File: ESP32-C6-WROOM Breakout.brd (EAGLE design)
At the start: 96.8 x 49.5 mm, 65 parts, among them J10 HP I2C, J11 LP I2C, J2 LP I2C, P1 GPIO-A2, P10 LP_I2C, P11 LiPo In, P2 GPIO-A1, P3 ADC, P4 O/P DRV, P5 CTRL, P6 HP_UART, P7 HP_I2C, P8 B2B-PH-K, P9 B2B-PH-K, U1 AP2112K-3.3TRG1, U2 ESP32-C6-WROOM-1-N4, U3 AP2112K-3.3TRG1LONG_PADS

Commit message: gitignore + WIP (close to candidate v1)
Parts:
- removed Q1, Q2, Q3, Q4: (no value), Master 2016:SOT23
- removed U1: AP2112K-3.3TRG1, AP2112K-3.3TRG1:SOT95P285X140-5N
- added J3: HP_UART, Connector:5P-2.54
- added Q6, Q7, Q8: (no value), Master 2016:SOT23_LONG
- U3: value AP2112K-3.3TRG1LONG_PADS -> AP2112
- moved P1 27.9 mm to (90.2, 3.81)
- moved JP7 10.2 mm to (64.8, 11.4)
- moved P2 10.2 mm to (64.8, 3.81)
- moved P6 10.2 mm to (78.7, 3.81)
- moved JP1 10.2 mm to (62.2, 11.4)
- moved JP8 10.2 mm to (67.3, 11.4)
- moved J10 7.75 mm to (28.6, 20.3)
- moved C7 6.75 mm to (32.4, 29.2), turned to 90 degrees
- moved U3 6.35 mm to (22.9, 29.2), turned to 270 degrees
- moved JP6 4.26 mm to (54.6, 23.5)
- moved C3 2.84 mm to (14.0, 29.2), flipped to the top
- moved C6 1.42 mm to (27.3, 29.2), turned to 90 degrees
- moved C8 1.27 mm to (19.1, 29.2), turned to 270 degrees
- moved D1 0.90 mm to (15.2, 37.5)
- moved P11 0.64 mm to (3.17, 44.5)
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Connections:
- net GND: now also J3.1; no longer U1.2
- net GPIO22: now also Q8.1; no longer Q2.1
- net GPIO23: now also Q6.1; no longer Q4.1
- net LP_GPIO4: now also Q7.1; no longer Q3.1
- net LP_GPIO5: no longer Q1.1
- net N$12: now also Q7.3; no longer Q3.3
- net N$13: no longer U1.5
- net N$15: now also Q6.3; no longer Q4.3
- net N$7: no longer Q1.3
- net RX: now also J3.4
- net TX: now also J3.5
- net UART_VCC: now also J3.3, Q8.3; no longer Q2.3
- net VCC: now also Q6.2, Q7.2, Q8.2; no longer Q1.2, Q2.2, Q3.2, Q4.2
- net VIN: no longer U1.1, U1.3
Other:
- board text added: "3V3"
- board text added: "ADC / #2"
- board text added: "GND"
- board text added: "SCL"
- board text added: "SDA"

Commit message: WIP getting there
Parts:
- added P12: Pwr Out, con-jst-ph:B3B-PH-K
- added P13: (no value), Master 2016:1X02
- added Q1: FDN338P, Master 2016:SOT23_LONG
- added R12, R13, R14, R15, R21: (no value), Master 2016:1206
- added R16, R17, R18, R19: 4k7, Master 2016:1206
- added R20: 10k, Master 2016:1206
- BAT1: value (none) -> 2-1775485-1
- C1, C2: value (none) -> 18p
- C3: value (none) -> 10u
- JP10: value BOOT -> (none)
- JP12: value (none) -> UART Vcc; device Master 2016:1X02 -> Connector:3P-2.54
- JP8: value (none) -> BOOT
- JP9: value (none) -> I_measure
- P1: value GPIO-A2 -> LP_I2C; device con-jst-eh:B3B-EH-A -> con-jst-eh:B4B-EH-A
- P10: value LP_I2C -> Pwr Sw 23; device con-jst-eh:B4B-EH-A -> con-jst-ph:B2B-PH-K
- P2: value GPIO-A1 -> HP_I2C; device con-jst-eh:B5B-EH-A -> con-jst-eh:B4B-EH-A
- P3: value ADC -> CTRL
- P5: value CTRL -> ADC; device con-jst-eh:B3B-EH-A -> con-jst-eh:B4B-EH-A
- P6: value HP_UART -> GPIO-A1; device con-jst-eh:B4B-EH-A -> con-jst-eh:B5B-EH-A
- P7: value HP_I2C -> HP_UART
- P8: value B2B-PH-K -> GPIO-A2; device con-jst-ph:B2B-PH-K -> con-jst-eh:B3B-EH-A
- P9: value B2B-PH-K -> Pwr Sw 22
- Q5, Q6, Q7, Q8: value (none) -> FDN338P
- R3, R5, R6, R8: value (none) -> 10k
- X1: value (none) -> CFS-20632768EZFB
- moved P10 90.4 mm to (92.7, 34.3), turned to 90 degrees
- moved P1 82.5 mm to (7.62, 3.81)
- moved P7 61.0 mm to (81.3, 3.81)
- moved JP10 48.6 mm to (88.9, 47.0)
- moved P2 44.4 mm to (20.3, 3.81)
- moved JP5 42.3 mm to (46.4, 12.1), turned to 90 degrees
- moved JP6 32.4 mm to (84.5, 10.8)
- moved JP8 30.0 mm to (43.2, 29.2), turned to 180 degrees
- moved JP7 27.8 mm to (84.5, 31.1), turned to 0 degrees
- moved P5 21.6 mm to (53.3, 3.81)
- moved P3 20.3 mm to (31.8, 3.81)
- moved P9 19.7 mm to (92.7, 13.3)
- moved JP12 18.5 mm to (95.9, 23.5)
- moved JP2 17.8 mm to (66.0, 11.4)
- moved JP3 15.9 mm to (68.6, 11.4), turned to 90 degrees
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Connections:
- new net LP_GPIO6: U2.6
- new net LP_GPIO7: U2.7
- new net N$9: P5.4, Q1.3
- new net PWR_SW_22: JP12.1, JP6.2, P9.2, Q8.3
- net ADC: now also P5.2; no longer P3.2
- net GND: now also JP2.2, JP3.2, P1.2, P10.1, P12.1, P2.2, P7.1; no longer JP10.2, JP7.2, P1.1, P10.2, P2.1, P7.2
- net GPIO10: now also P2.3, R18.1; no longer P7.3
- net GPIO11: now also P2.4, R19.1; no longer P7.4
- net GPIO15_R: now also JP10.2, P3.2; no longer JP11.2, P5.2
- net GPIO18: now also P6.2; no longer P2.2
- net GPIO19: now also JP2.1, P6.3; no longer JP7.1, P2.3
- net GPIO20: now also JP3.1, P6.4; no longer JP8.1, P2.4
- net GPIO21: now also P6.5, R2.1; no longer P2.5
- net GPIO22: now also P8.3, R15.1, R15.2; no longer P1.3, R2.1
- net GPIO23: now also P8.2, R14.1, R14.2; no longer P1.2
- net GPIO6: now also P1.4, Q1.1, R16.2, R20.1, R21.1, R21.2; no longer P10.4, U2.6
- net GPIO7: now also P1.3, R17.2; no longer P10.3, U2.7
- net GPIO8: now also P13.1; no longer JP6.1
- net GPIO9: now also P13.2; no longer JP6.2
- net LP_GPIO3: now also P3.3; no longer P5.3
- net LP_GPIO4: now also R13.1, R13.2
- net LP_GPIO5: now also JP5.2, R12.1, R12.2; no longer JP2.2
- net LP_GPIO5_P: now also JP5.1; no longer JP2.1
- net N$1: now also JP8.1; no longer JP10.1
- net N$10: now also JP11.2; no longer JP12.2
- net N$11: now also JP11.1; no longer JP12.1
- net N$15: now also JP7.2, P10.2; no longer JP5.2, P9.2
- net N$8: now also JP10.1; no longer JP11.1
- net RX: now also P7.3; no longer P6.3
- net TX: now also P7.2; no longer P6.2
- net UART_VCC: now also JP12.2, P7.4; no longer JP3.2, P6.4, P8.2, Q8.3
- net VCC: now also JP12.3, JP6.1, JP7.1, P1.1, P12.2, P2.1, P5.3, Q1.2, R16.1, R17.1, R18.2, R19.2, R20.2; no longer JP3.1, JP5.1, P10.1, P3.3, P7.1
- net VIN: now also P12.3
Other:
- board size 96.8 x 49.5 mm -> 99 x 49.5 mm
- board text added: "ADC"
- board text removed: "ADC / #2"

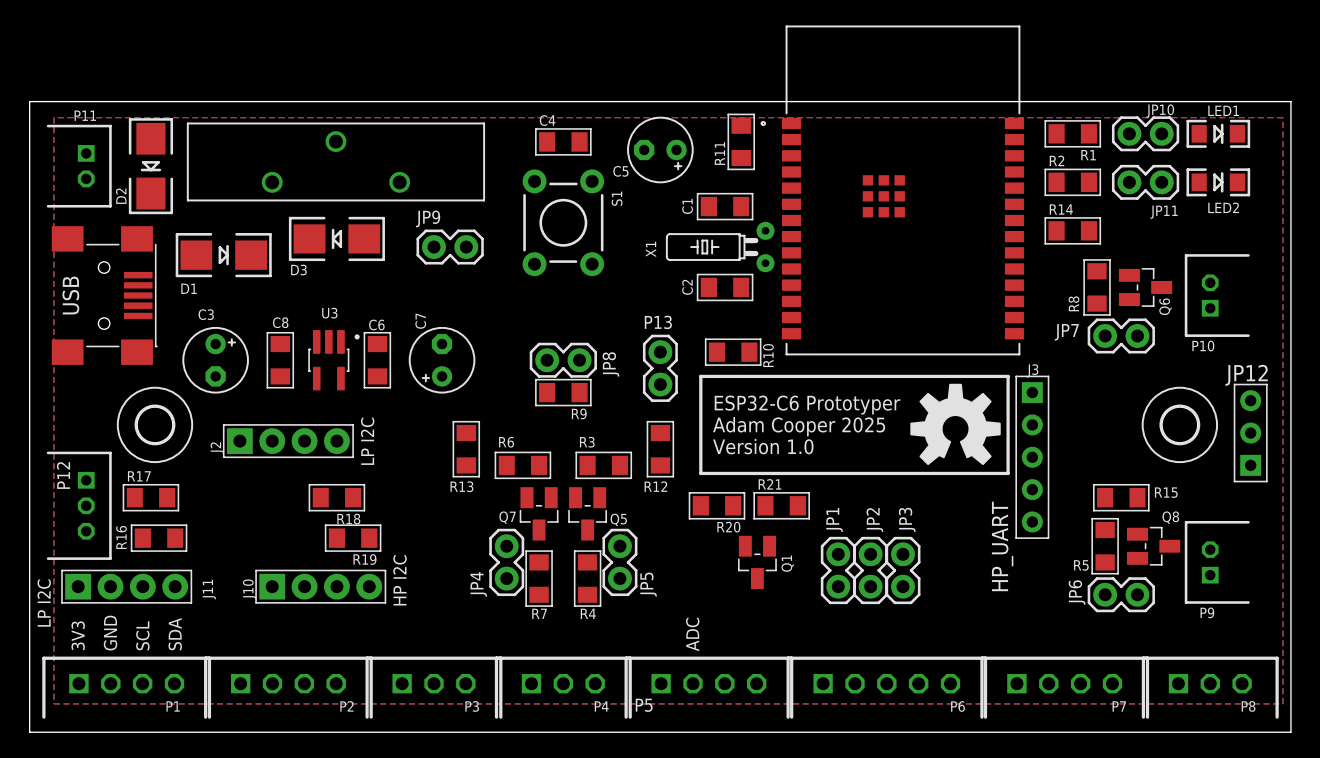
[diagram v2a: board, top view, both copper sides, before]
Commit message: move ADC and add o/p drive caps
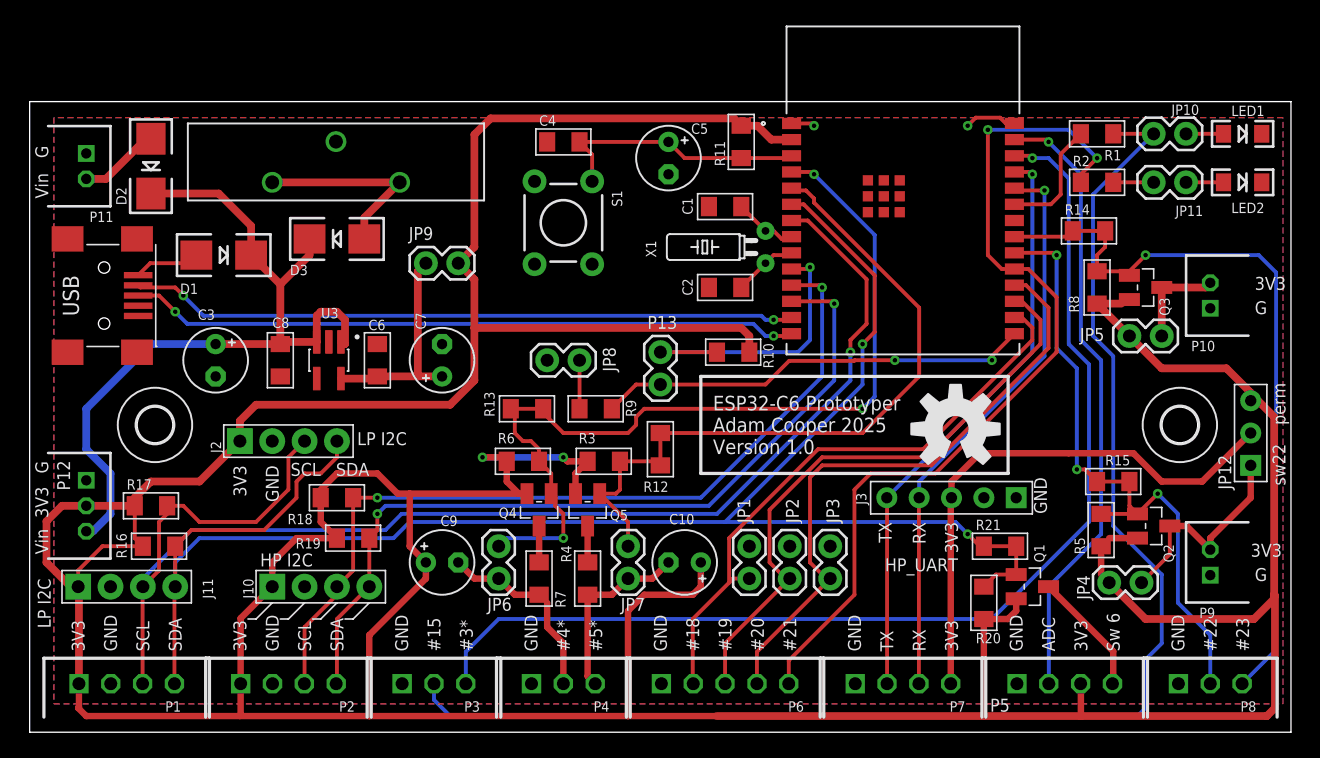
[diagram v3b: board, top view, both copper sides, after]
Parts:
- removed Q7, Q8: FDN338P, Master 2016:SOT23_LONG
- added C10, C9: 10u, Master 2016:E2,5-5
- added LOGO2: OSHW-LOGOL, Master 2016:OSHW-LOGO-L
- added Q2, Q4: FDN338P, Master 2016:SOT23_LONG
- P4: value O/P DRV -> HI DRV/CNT
- moved JP6 47.6 mm to (36.8, 12.1), turned to 90 degrees
- moved JP4 47.3 mm to (84.8, 11.7), turned to 0 degrees
- moved JP5 44.3 mm to (86.4, 31.1), turned to 0 degrees
- moved JP7 42.0 mm to (47.0, 12.1), turned to 90 degrees
- moved P5 27.9 mm to (81.3, 3.81)
- moved R20 22.3 mm to (74.9, 10.2), turned to 270 degrees
- moved Q1 21.7 mm to (78.7, 11.4), turned to 270 degrees
- moved R21 17.4 mm to (76.2, 14.6)
- moved P6 12.7 mm to (54.6, 3.81)
- moved P7 12.7 mm to (68.6, 3.81)
- moved J3 7.10 mm to (72.4, 18.4), turned to 270 degrees
- moved JP1 7.01 mm to (56.5, 12.1)
- moved JP2 6.38 mm to (59.7, 12.1)
- moved JP3 5.75 mm to (62.9, 12.1)
- moved R13 5.72 mm to (39.1, 25.4), turned to 0 degrees
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- renumbered Q6 to Q3
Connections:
- net N$16 renamed GPIO15
- removed net GPIO6: J11.4, J2.4, P1.4, Q1.1, R16.2, R20.1, R21.1, R21.2
- removed net GPIO7: J11.3, J2.3, P1.3, R17.2
- net GPIO22: now also P8.2, Q2.1; no longer P8.3, Q8.1
- net GPIO23: now also P8.3; no longer P8.2
- net LP_GPIO4: now also JP6.2, Q4.1; no longer JP4.2, Q7.1
- net LP_GPIO4_P: now also C9.-, JP6.1; no longer JP4.1
- net LP_GPIO5: now also JP7.2; no longer JP5.2
- net LP_GPIO5_P: now also C10.-, JP7.1; no longer JP5.1
- net LP_GPIO6: now also J11.4, J2.4, P1.4, Q1.1, R16.2, R20.1, R21.1, R21.2
- net LP_GPIO7: now also J11.3, J2.3, P1.3, R17.2
- net N$12: now also Q4.3; no longer Q7.3
- net N$15: now also JP5.2; no longer JP7.2
- net PWR_SW_22: now also JP4.2, Q2.3; no longer JP6.2, Q8.3
- net VCC: now also C10.+, C9.+, JP4.1, JP5.1, Q2.2, Q4.2; no longer JP6.1, JP7.1, Q7.2, Q8.2
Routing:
- net VCC: track 0.00 -> 403.2 mm, vias 0 -> 2
- net LP_GPIO6: track 0.00 -> 136.7 mm, vias 0 -> 2
- net GPIO15_R: track 0.00 -> 110.9 mm
- net LP_GPIO7: track 0.00 -> 109.1 mm, vias 0 -> 1
- net LP_GPIO3: track 0.00 -> 88.3 mm, vias 0 -> 1
- net GPIO21: track 0.00 -> 70.9 mm, vias 0 -> 2
- net LP_GPIO4: track 0.00 -> 70.0 mm, vias 0 -> 3
- net GPIO10: track 0.00 -> 66.4 mm, vias 0 -> 2
- net GPIO11: track 0.00 -> 64.4 mm, vias 0 -> 2
- net VIN: track 0.00 -> 62.4 mm
- net GPIO23: track 0.00 -> 60.3 mm, vias 0 -> 1
- net LP_GPIO5: track 0.00 -> 56.5 mm
- net GPIO13: track 0.00 -> 52.7 mm, vias 0 -> 2
- net GPIO12: track 0.00 -> 52.5 mm, vias 0 -> 2
- net GPIO22: track 0.00 -> 49.9 mm, vias 0 -> 3
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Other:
- board text added: "#10"
- board text added: "#11"
- board text added: "#15"
- board text added: "#18"
- board text added: "#19"
- board text added: "#2*"
- board text added: "#20"
- board text added: "#21"
- board text added: "#22"
- board text added: "#23"
- board text added: "#3*"
- board text added: "#4*"
- board text added: "#5*"
- board text added: "#6*"
- board text added: "#7*"
- board text added: "G"
- board text added: "RX"
- board text added: "Sw 6"
- board text added: "TX"
- board text added: "Vin"
- board text added: "perm"
- board text added: "sw22"

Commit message: 32kHz crystal ground plane separation
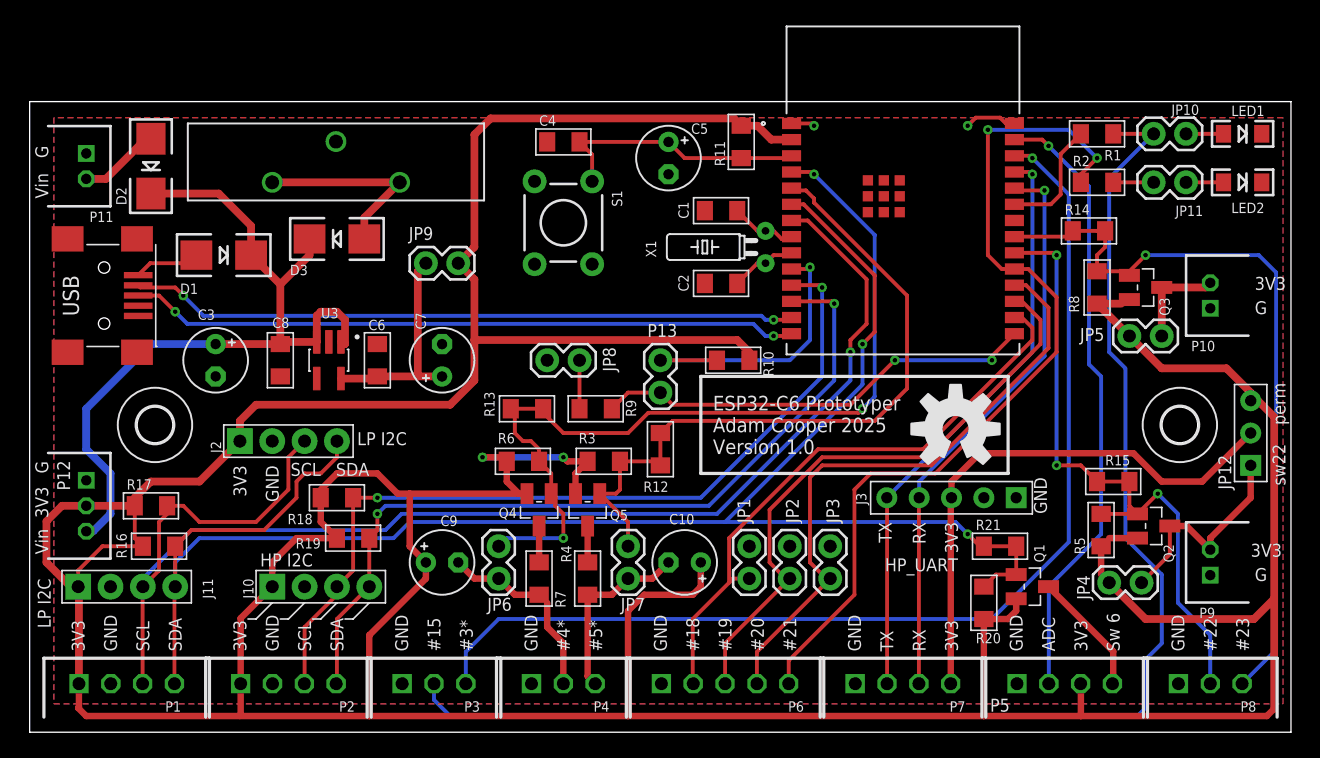
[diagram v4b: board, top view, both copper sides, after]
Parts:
- moved P13 0.63 mm to (49.5, 29.2)
- moved R10 0.63 mm to (55.2, 29.2)
- moved C2 0.45 mm to (54.3, 35.2)
- moved C1 0.45 mm to (54.3, 41.0)
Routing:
- net LP_GPIO3: track 88.3 -> 86.2 mm
- net GPIO15_R: track 110.9 -> 109.9 mm
- net VCC: track 403.2 -> 402.3 mm
- net LP_GPIO5: track 56.5 -> 55.7 mm
- net GPIO9: track 34.2 -> 35.0 mm
- net GPIO22: track 49.9 -> 50.7 mm

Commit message: close to v1 rev
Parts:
- removed Q5: FDN338P, Master 2016:SOT23_LONG
- added D4: SL115B, Master 2016:DO-214AA
- added J4, J5: (no value), Connector:1P-65/35MIL
- added JP13: PS Src, Connector:3P-2.54
- added JP14: I_measure, Master 2016:1X02
- added P14: Backup, con-jst-ph:B2B-PH-K
- C10: device Master 2016:E2,5-5 -> Master 2016:1206
- C3, C9: value 10u -> 100n; device Master 2016:E2,5-5 -> Master 2016:1206
- C6: value 100n -> 1u
- C7: value 10u -> 1u; device Master 2016:E2,5-5 -> Master 2016:1206
- C8: value 100n -> 10u
- J2: value LP I2C -> HP I2C
- JP3: value (none) -> BOOT
- JP8: value BOOT -> (none)
- JP9: value I_measure -> (none)
- P10: device con-jst-ph:B2B-PH-K -> con-jst-ph:B3B-PH-K
- P5: device con-jst-eh:B4B-EH-A -> con-jst-eh:B3B-EH-A
- P6: device con-jst-eh:B5B-EH-A -> con-jst-eh:B6B-EH-A
- R20: value 10k -> 2k2
- R21: value (none) -> 1k
- moved R21 63.3 mm to (15.2, 31.8)
- moved R20 62.5 mm to (15.2, 28.6), turned to 0 degrees
- moved C9 60.9 mm to (83.2, 47.0)
- moved Q3 50.7 mm to (40.0, 17.5), turned to 180 degrees
- moved C3 45.2 mm to (56.8, 45.4)
- moved C10 28.0 mm to (79.4, 14.6), turned to 0 degrees
- moved JP9 27.6 mm to (47.0, 14.3), turned to 270 degrees
- moved JP3 26.1 mm to (43.2, 29.2), turned to 180 degrees
- moved Q1 24.8 mm to (86.7, 34.9)
- moved R11 20.7 mm to (36.2, 40.0), turned to 180 degrees
- moved C8 18.2 mm to (34.3, 18.4), turned to 180 degrees
- moved JP8 16.2 mm to (36.8, 14.3), turned to 270 degrees
- moved C6 6.35 mm to (21.0, 29.2), turned to 270 degrees
- moved R2 4.72 mm to (87.3, 40.0)
- moved R1 3.93 mm to (82.9, 43.2)
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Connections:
- new net N$14: JP13.3, P10.3
- new net N$16: J4.P$1, JP1.1
- new net N$2: D2.A, P11.1
- new net N$5: JP13.2, JP5.1, Q1.2, R8.2
- net ADC: now also C9.1, R20.1, R21.1
- net GND: now also C10.1, C3.2, C7.2, C9.2, P10.2, P11.2, P12.2, P14.2, P9.2, R20.2; no longer C3.-, C7.-, JP8.2, P10.1, P11.1, P12.1, P9.1
- net GPIO10: now also J2.3
- net GPIO11: now also J2.4
- net GPIO18: no longer JP1.1
- net GPIO19: no longer JP2.1
- net GPIO20: no longer JP3.1
- net GPIO23: now also Q1.1; no longer Q3.1
- net LP_GPIO4: now also Q3.1; no longer Q4.1
- net LP_GPIO4_P: now also JP8.2; no longer C9.-
- net LP_GPIO5: now also Q4.1; no longer Q5.1
- net LP_GPIO5_P: now also JP9.2; no longer C10.-
- net LP_GPIO6: no longer J2.4, Q1.1, R20.1, R21.1, R21.2
- net LP_GPIO7: no longer J2.3
- net N$1: now also JP3.1; no longer JP8.1
- net N$12: now also JP8.1, Q3.3; no longer Q4.3
- net N$13: now also C7.1, D3.C, JP14.1; no longer C6.1, C7.+, JP9.1
- net N$15: now also P10.1, Q1.3; no longer P10.2, Q3.3
- net N$4: now also D4.A, P14.1; no longer D2.A, P11.2
- net N$7: now also JP9.1, Q4.3; no longer Q5.3
- net N$9: now also J5.P$1, JP2.1; no longer P5.4, Q1.3
- net PWR_SW_22: now also P9.1; no longer P9.2
- net VCC: now also C10.2, C3.1, C8.1, JP13.1, JP14.2, P12.1, P6.6; no longer C10.+, C9.+, JP5.1, JP9.2, P12.2, Q1.2, Q5.2, R20.2, R8.2
- net VIN: now also C6.1, D4.C, R21.2; no longer C3.+, C8.1, D3.C
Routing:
- net ADC: track 48.5 -> 173.5 mm, vias 1 -> 2
- net LP_GPIO6: track 136.7 -> 89.7 mm, vias 2 -> 1
- net VCC: track 402.3 -> 366.8 mm
- net N$5: track 0.00 -> 23.0 mm
- net GPIO15_R: track 109.9 -> 89.8 mm, vias 0 -> 1
- net LP_GPIO7: track 109.1 -> 93.0 mm
- net CHIP_EN: track 20.9 -> 29.7 mm
- net GPIO11: track 64.4 -> 71.9 mm
- net N$9: track 9.75 -> 2.54 mm
- net GPIO10: track 66.4 -> 73.3 mm
- net GND: track 5.96 -> 12.5 mm, vias 2 -> 6
- net GPIO21: track 70.9 -> 77.1 mm
- net N$2: track 0.00 -> 5.56 mm
- net N$14: track 0.00 -> 4.88 mm
- net GPIO23: track 60.3 -> 64.7 mm
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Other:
- board text added: "Cut trace if using ADC input"
- board text added: "ESP32-C6-WROOM-1"
- board text added: "Ext"
- board text removed: "Sw 6"

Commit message: Pre-panelisation final v1
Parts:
- moved C10 0.63 mm to (79.4, 14.0)
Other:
- board text removed: "ESP32-C6-WROOM-1"
